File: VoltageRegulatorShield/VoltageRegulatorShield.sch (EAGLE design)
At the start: 1 part

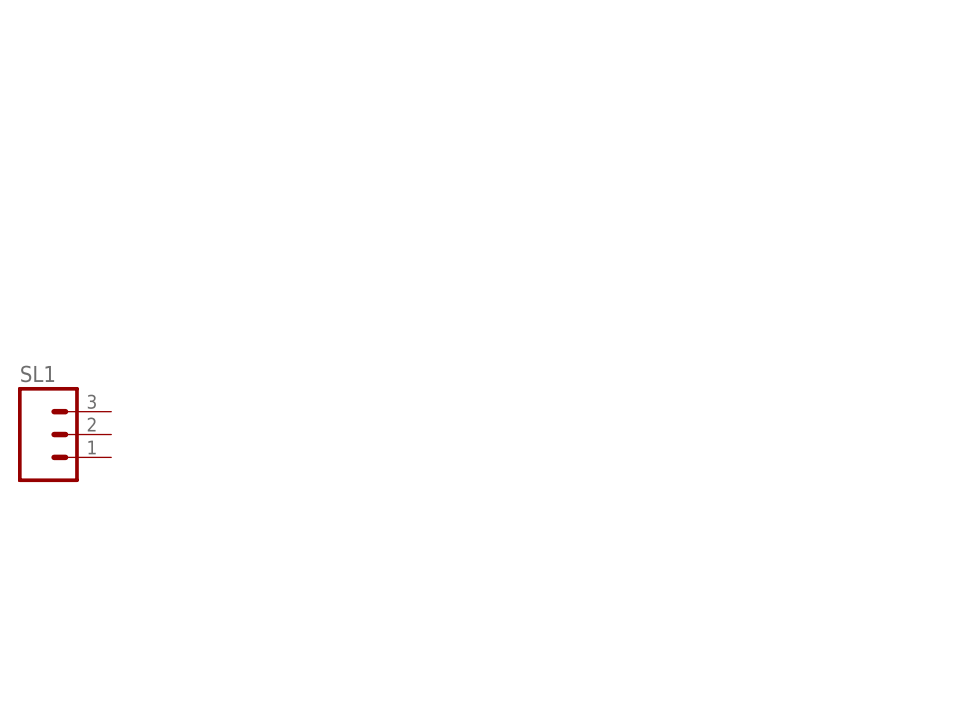
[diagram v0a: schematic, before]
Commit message: First version of Voltage Regulator test board
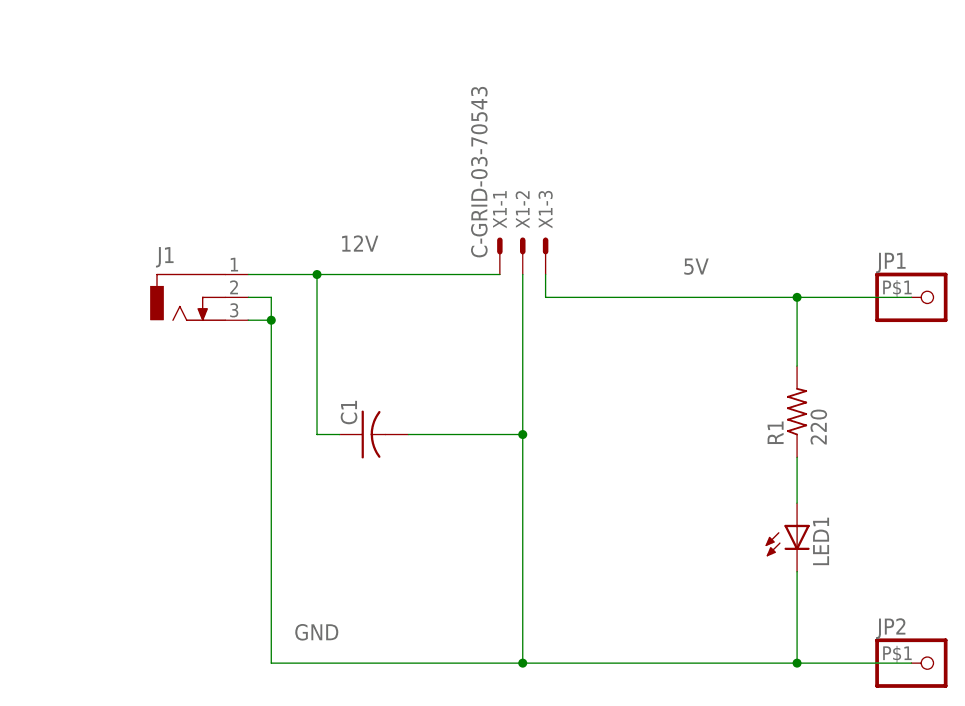
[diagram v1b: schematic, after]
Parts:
- removed SL1: (no value), con-amp-quick:M03
- added C1: (no value), adafruit:C-US025-025X050
- added J1: (no value), con-jack:DCJ0303
- added JP1, JP2: (no value), adafruit:PINHD-1X1-BIGPOGO
- added LED1: (no value), adafruit:LED5MM
- added R1: 220, adafruit:R-US_V234/12
- added X1: C-GRID-03-70543, con-molex:C-GRID-03-70543
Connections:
- new net 12V: C1.1, J1.1, X1-1.S
- new net 5V: JP1.1, R1.2, X1-3.S
- new net GND: C1.2, J1.2, J1.3, JP2.1, LED1.C, X1-2.S
- new net N$1: LED1.A, R1.1
